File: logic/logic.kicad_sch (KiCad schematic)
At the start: 15 parts, among them J1 DIN41612_03x32_ABC, J2 Conn_02x05_Odd_Even, J3 Conn_02x05_Odd_Even, U1 TPIC6595, U2 TPIC6595, U3 TPIC6595, U4 TPIC6595, U5 TPIC6595, U6 TPIC6595, U7 TPIC6595, U8 TPIC6595, U9 74HCT244

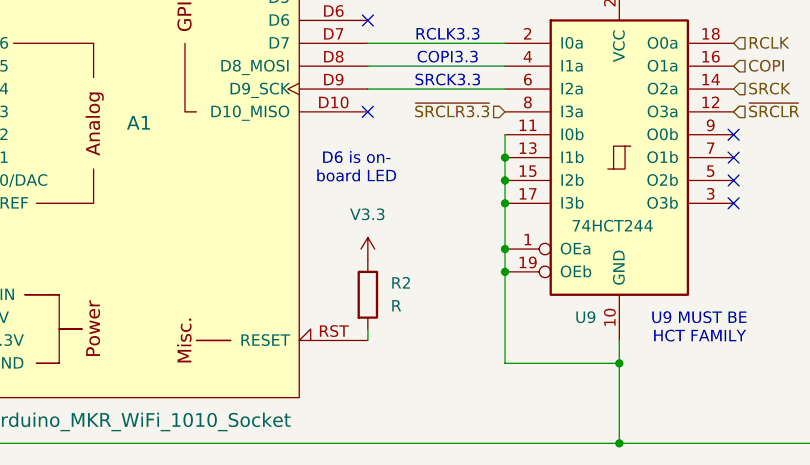
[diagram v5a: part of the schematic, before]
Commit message: Ongoing development. Add shunt resistors to display board.
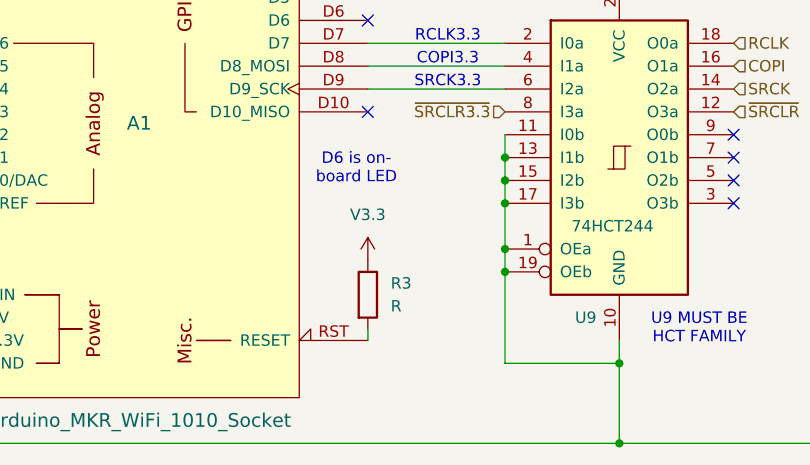
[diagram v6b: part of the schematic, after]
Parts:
- renumbered R2 to R3
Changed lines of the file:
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@@
 		(dnp no)
 		(fields_autoplaced yes)
-		(property "Reference" "R2"
+		(property "Reference" "R3"
 			(at 80.01 184.1499 0)
 			(effects
@@
 			(project "logic"
 				(path "/4078bfcf-e5c1-4f0e-b66f-b232c5a6fa8f"
-					(reference "R2")
+					(reference "R3")
 					(unit 1)
 				)

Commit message: Ongoing development
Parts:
- U1, U2, U3, U4, U5, U6, U7, U8: footprint Package_DIP:DIP-20_W7.62mm_Socket -> Package_DIP:DIP-20_W7.62mm_Socket_LongPads
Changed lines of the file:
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@@
 			)
 		)
-		(property "Footprint" "Package_DIP:DIP-20_W7.62mm_Socket"
+		(property "Footprint" "Package_DIP:DIP-20_W7.62mm_Socket_LongPads"
 			(at 158.75 59.69 0)
 			(effects
@@
 			)
 		)
-		(property "Footprint" "Package_DIP:DIP-20_W7.62mm_Socket"
+		(property "Footprint" "Package_DIP:DIP-20_W7.62mm_Socket_LongPads"
 			(at 110.49 59.69 0)
 			(effects
@@
 			)
 		)
-		(property "Footprint" "Package_DIP:DIP-20_W7.62mm_Socket"
+		(property "Footprint" "Package_DIP:DIP-20_W7.62mm_Socket_LongPads"
 			(at 62.23 59.69 0)
 			(effects
@@
 			)
 		)
-		(property "Footprint" "Package_DIP:DIP-20_W7.62mm_Socket"
+		(property "Footprint" "Package_DIP:DIP-20_W7.62mm_Socket_LongPads"
 			(at 125.73 153.67 0)
 			(effects
@@
 			)
 		)
-		(property "Footprint" "Package_DIP:DIP-20_W7.62mm_Socket"
+		(property "Footprint" "Package_DIP:DIP-20_W7.62mm_Socket_LongPads"
 			(at 255.27 59.69 0)
 			(effects
@@
 			)
 		)
-		(property "Footprint" "Package_DIP:DIP-20_W7.62mm_Socket"
+		(property "Footprint" "Package_DIP:DIP-20_W7.62mm_Socket_LongPads"
 			(at 222.25 153.67 0)
 			(effects
@@
 			)
 		)
-		(property "Footprint" "Package_DIP:DIP-20_W7.62mm_Socket"
+		(property "Footprint" "Package_DIP:DIP-20_W7.62mm_Socket_LongPads"
 			(at 207.01 59.69 0)
 			(effects
@@
 			)
 		)
-		(property "Footprint" "Package_DIP:DIP-20_W7.62mm_Socket"
+		(property "Footprint" "Package_DIP:DIP-20_W7.62mm_Socket_LongPads"
 			(at 173.99 153.67 0)
 			(effects

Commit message: Ongoing development - logic board routing
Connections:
- net GND: now also J1.b17 (Pin_b17), J1.b18 (Pin_b18), J1.b19 (Pin_b19), J1.b20 (Pin_b20), J1.b21 (Pin_b21), J1.b22 (Pin_b22), J1.b23 (Pin_b23), J1.b24 (Pin_b24), J1.b25 (Pin_b25), J1.b26 (Pin_b26), J1.b27 (Pin_b27), J1.b28 (Pin_b28), J1.b29 (Pin_b29), J1.b30 (Pin_b30), J1.b31 (Pin_b31), J1.b32 (Pin_b32)
- net V170: no longer J1.b17 (Pin_b17), J1.b18 (Pin_b18), J1.b19 (Pin_b19), J1.b20 (Pin_b20), J1.b21 (Pin_b21), J1.b22 (Pin_b22), J1.b23 (Pin_b23), J1.b24 (Pin_b24), J1.b25 (Pin_b25), J1.b26 (Pin_b26), J1.b27 (Pin_b27), J1.b28 (Pin_b28), J1.b29 (Pin_b29), J1.b30 (Pin_b30), J1.b31 (Pin_b31), J1.b32 (Pin_b32)
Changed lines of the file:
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@@
 	)
 	(junction
-		(at 111.76 81.28)
-		(diameter 0)
-		(color 0 0 0 0)
-	)
-	(junction
 		(at 137.16 81.28)
 		(diameter 0)
@@
 		)
 	)
-	(wire
-		(pts
-			(xy 111.76 81.28) (xy 111.76 99.06)
-		)
-		(stroke
-			(width 0)
-			(type default)
-		)
-	)
 	(bus
 		(pts
@@
 	(wire
 		(pts
+			(xy 111.76 99.06) (xy 111.76 100.33)
+		)
+		(stroke
+			(width 0)
+			(type default)
+		)
+	)
+	(wire
+		(pts
 			(xy 165.1 96.52) (xy 165.1 111.76)
 		)
@@
 	(wire
 		(pts
-			(xy 107.95 81.28) (xy 111.76 81.28)
+			(xy 107.95 81.28) (xy 116.84 81.28)
 		)
 		(stroke
@@
 	(wire
 		(pts
-			(xy 116.84 81.28) (xy 111.76 81.28)
-		)
-		(stroke
-			(width 0)
-			(type default)
-		)
-	)
-	(wire
-		(pts
 			(xy 203.2 50.8) (xy 210.82 50.8)
 		)
@@
 					(unit 1)
 				)
+			)
+		)
+	)
+	(symbol
+		(lib_id "power:GND")
+		(at 111.76 100.33 0)
+		(unit 1)
+		(exclude_from_sim no)
+		(in_bom yes)
+		(on_board yes)
+		(dnp no)
+		(fields_autoplaced yes)
+		(property "Reference" "#PWR010"
+			(at 111.76 106.68 0)
+			(effects
+				(font
+					(size 1.27 1.27)
+				)
+				(hide yes)
+			)
+		)
+		(property "Value" "GND"
+			(at 111.76 105.41 0)
+			(effects
+				(font
+					(size 1.27 1.27)
+				)
+			)
+		)
+		(property "Footprint" ""
+			(at 111.76 100.33 0)
+			(effects
+				(font
+					(size 1.27 1.27)
+				)
+				(hide yes)
+			)
+		)
+		(property "Datasheet" ""
+			(at 111.76 100.33 0)
+			(effects
+				(font
+					(size 1.27 1.27)
+				)
+				(hide yes)
+			)
+		)
+		(property "Description" "Power symbol creates a global label with name \"GND\" , ground"
+			(at 111.76 100.33 0)
+			(effects
+				(font
+					(size 1.27 1.27)
+				)
+				(hide yes)
+			)
+		)
+		(pin "1"
+		)
+		(instances
+			(project "logic"
+				(path "/4078bfcf-e5c1-4f0e-b66f-b232c5a6fa8f"
+					(reference "#PWR010")
+					(unit 1)
+				)
